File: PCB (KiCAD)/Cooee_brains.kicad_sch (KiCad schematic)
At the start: 35 parts, among them J1 USB4105-GF-A, J2 Conn_Coaxial, J3 503398-1892, J4 Conn_01x14_Socket, J5 Conn_01x02_Pin, J6 Conn_Coaxial, J7 Conn_01x04_Pin, J9 Conn_01x05_Socket, SW1 Prog, SW2 Reset, U1 AMS1117-3.3, U2 ESP32-S3-WROOM-1-N8, U3 MAX98357AETE_T, U6 INTERFACE-CP2102-GMR_QFN28_, U8 RA-01H

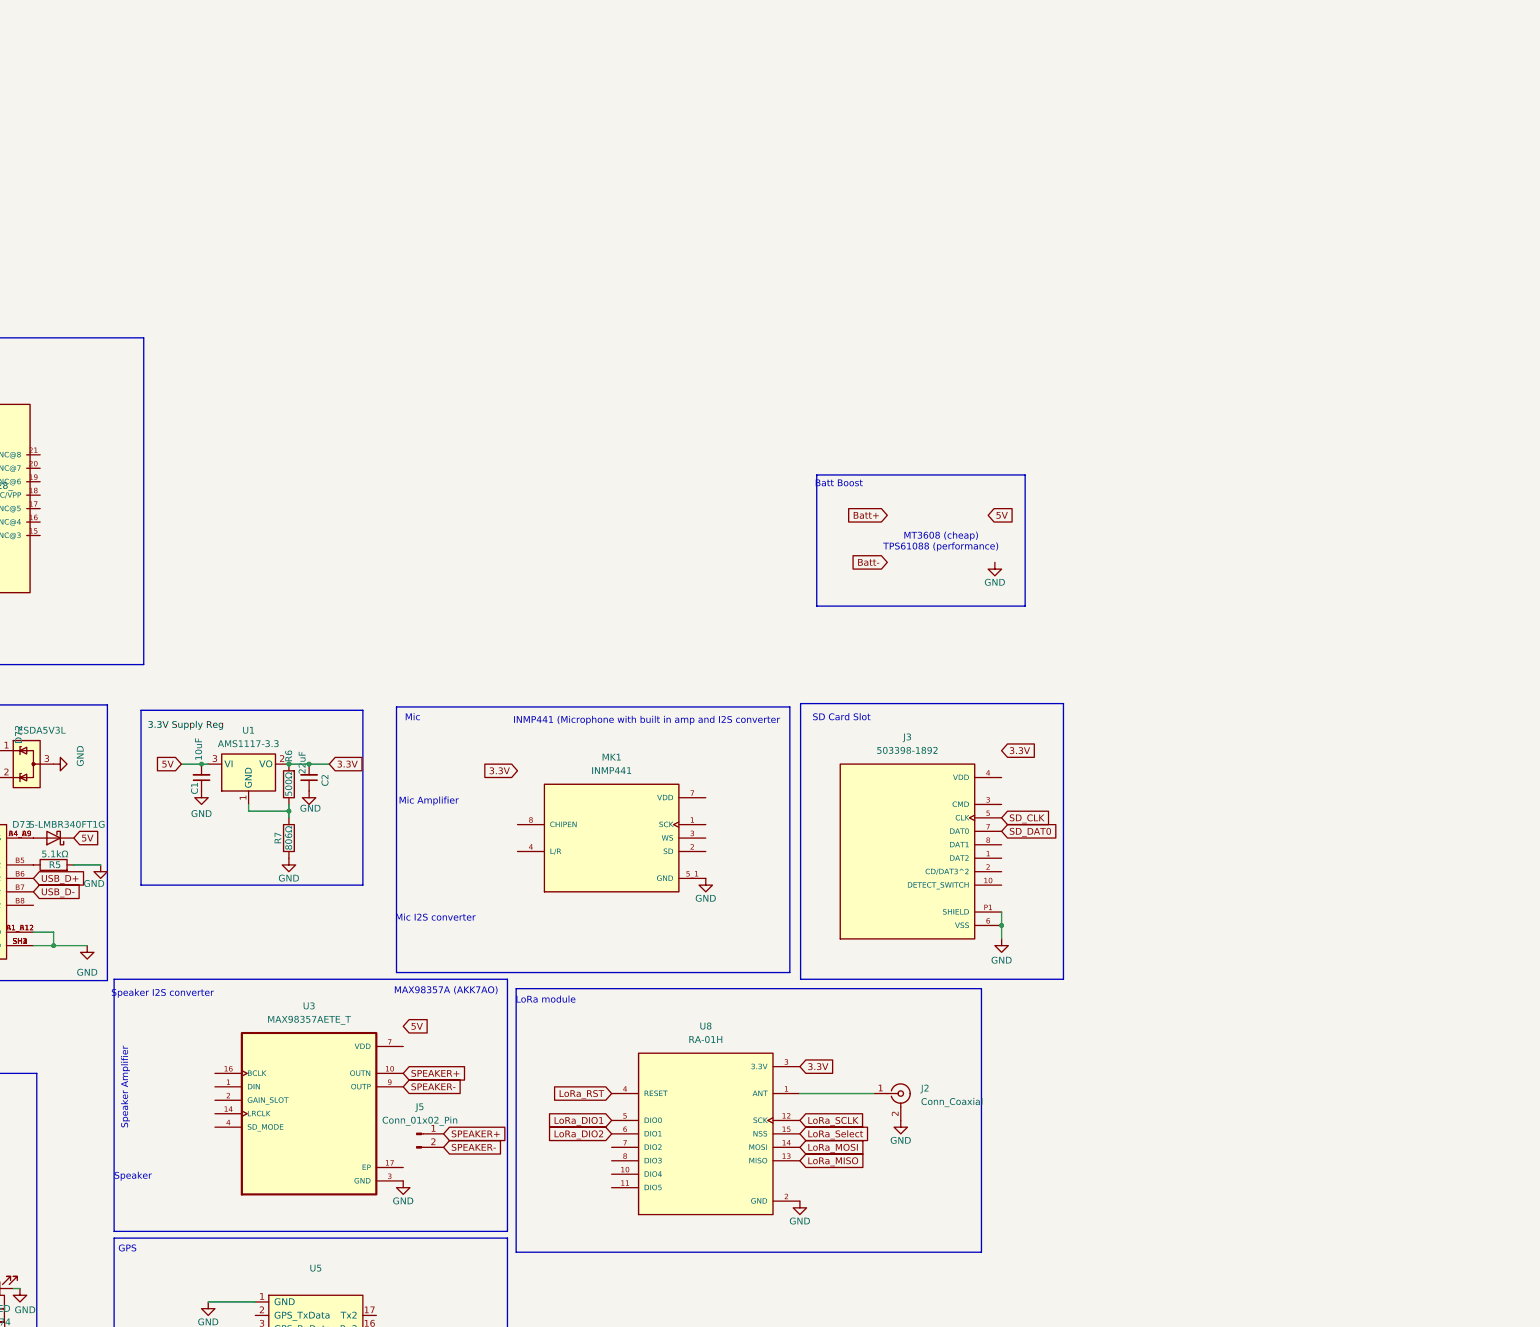
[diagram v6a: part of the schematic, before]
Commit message: finalized next prototype of keyboard PCB, ready to order
finalized next prototype of keyboard PCB, ready to order
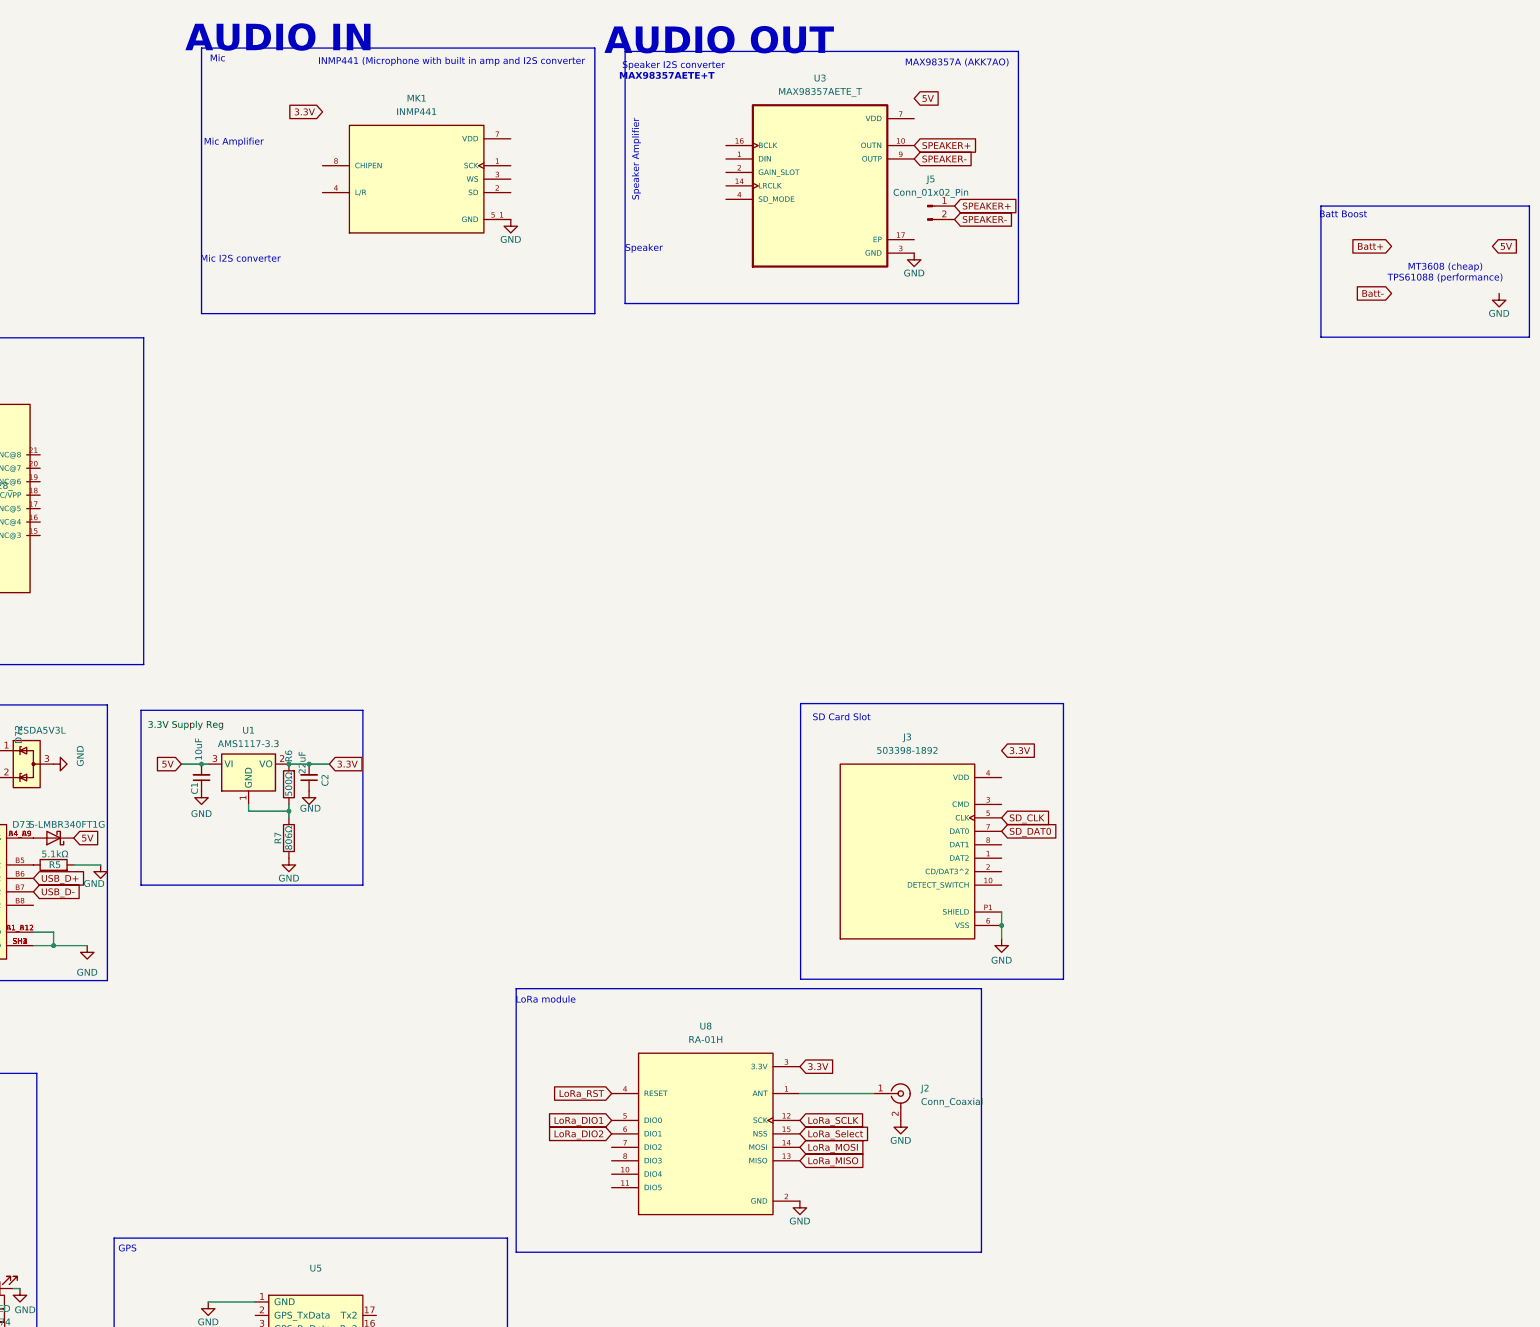
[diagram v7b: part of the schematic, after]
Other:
- note added: "AUDIO IN"
- note added: "AUDIO OUT"
- note added: "MAX98357AETE+T"
- moved on the sheet: J5, MK1, U3

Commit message: pcb layout work on phone motherboard
pcb layout work on phone motherboard
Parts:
- added Keyboard1: Keyboard, TestPoint:TestPoint_Pad_1.0x1.0mm, symbol Connector:TestPoint
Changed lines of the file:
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@@
+	)
+	(symbol
+		(lib_id "Connector:TestPoint")
+		(at -13.97 -49.53 0)
+		(unit 1)
+		(exclude_from_sim no)
+		(in_bom yes)
+		(on_board yes)
+		(dnp no)
+		(fields_autoplaced yes)
+		(property "Reference" "Keyboard1"
+			(at -10.16 -54.1021 0)
+			(effects
+				(font
+					(size 1.27 1.27)
+				)
+				(justify left)
+			)
+		)
+		(property "Value" "Keyboard"
+			(at -10.16 -51.5621 0)
+			(effects
+				(font
+					(size 1.27 1.27)
+				)
+				(justify left)
+			)
+		)
+		(property "Footprint" "TestPoint:TestPoint_Pad_1.0x1.0mm"
+			(at -8.89 -49.53 0)
+			(effects
+				(font
+					(size 1.27 1.27)
+				)
+				(hide yes)
+			)
+		)
+		(property "Datasheet" "~"
+			(at -8.89 -49.53 0)
+			(effects
+				(font
+					(size 1.27 1.27)
+				)
+				(hide yes)
+			)
+		)
+		(property "Description" "test point"
+			(at -13.97 -49.53 0)
+			(effects
+				(font
+					(size 1.27 1.27)
+				)
+				(hide yes)
+			)
+		)
+		(pin "1"
+		)
+		(instances
+			(project ""
+				(path "/38f2fbf3-bfbd-4714-9298-32093c806bb8"
+					(reference "Keyboard1")
+					(unit 1)
+				)
+			)
+		)
 	)
 	(symbol
